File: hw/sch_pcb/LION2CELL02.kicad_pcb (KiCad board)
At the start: 2 copper layers, 80.8 x 60.5 mm, 100 parts, among them J1 USBC_USB4105-GF-A, J10 HEADER_2x01_PARALLEL, J11 HEADER_1x02, J12 HEADER_2x05_PARALLEL, J2 CONN1_1, J3 CONN1_1, J4 JUMP_4X2, J6 HEADER_2x01_PARALLEL, J7 HEADER_2x01_PARALLEL, J8 CONN1_1, J9 CONN1_1, Q1 DMT31M7LPS, Q2 AP2305AGN-HF-3, Q3 DMT31M7LPS, Q5 DMT31M7LPS, SW1 SW_Push, SW2 SW_Push, U1 BQ25792RQMR1, U2 LMR14050, U3 BQ40z50-R2

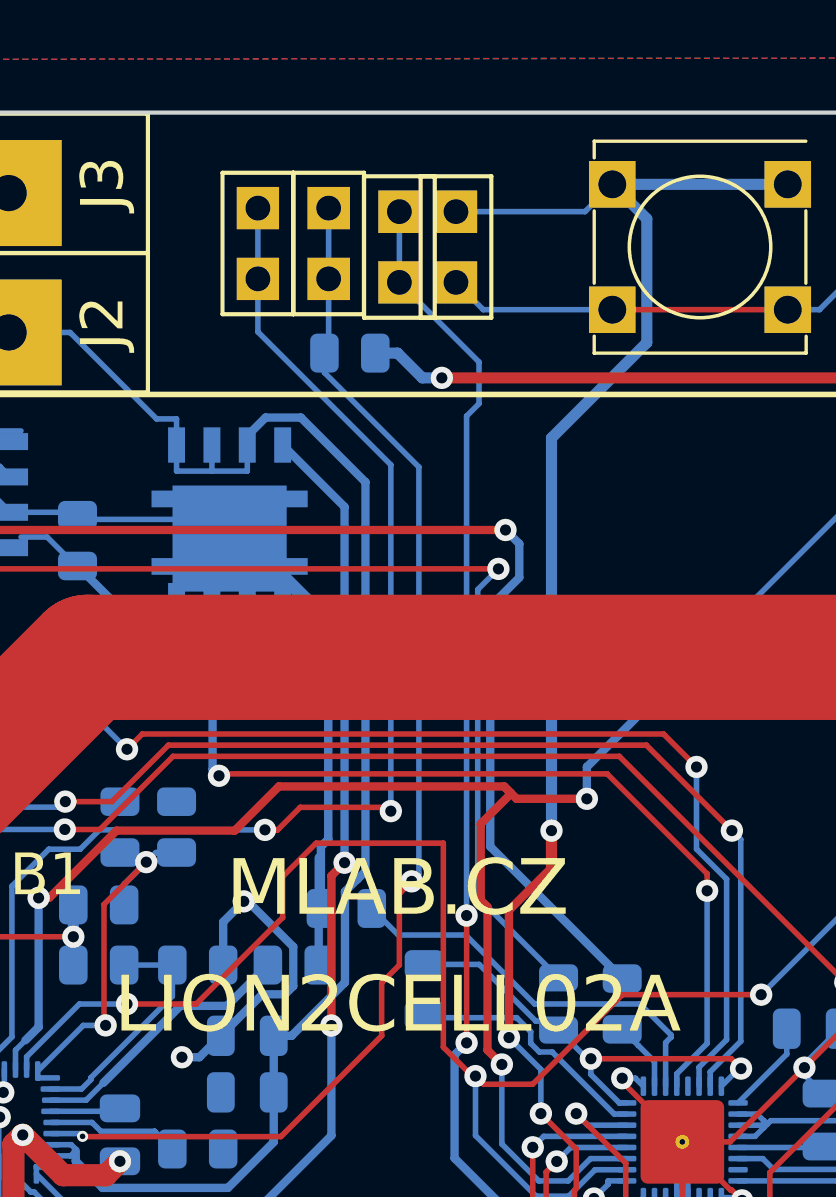
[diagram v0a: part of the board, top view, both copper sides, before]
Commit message: Reduce complexity of layout.
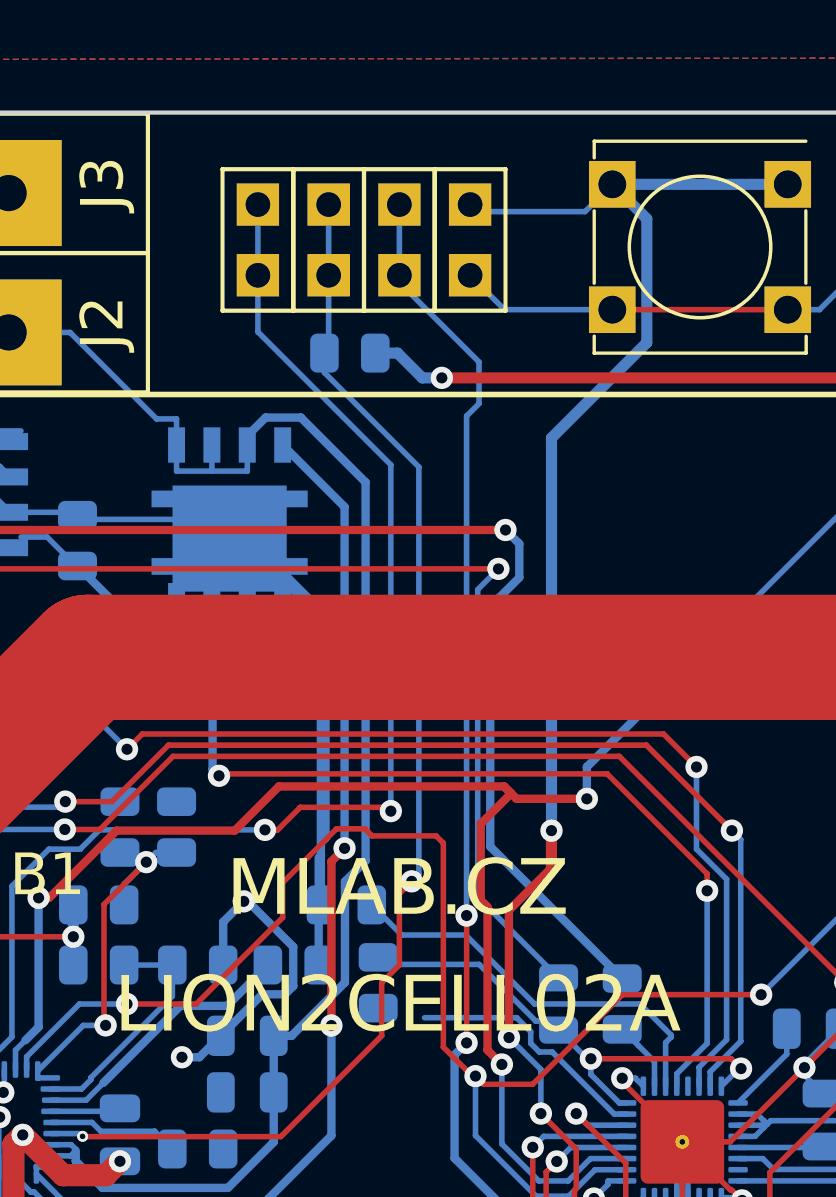
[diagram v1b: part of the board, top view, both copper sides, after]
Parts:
- moved TH4 1.67 mm to (147.7, 106.0)
- moved J11 0.57 mm to (151.0, 79.3)
- moved J10 0.25 mm to (148.5, 79.3)
- moved R24 0.13 mm to (146.6, 103.2)
- moved J6 0.13 mm to (146.0, 79.3)
- moved J7 0.13 mm to (143.4, 79.3)
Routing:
- net /Fuel Gauge/BAT: track 15.7 -> 17.5 mm
- net Net-(U3-~{PRES/SHDWN}): track 56.4 -> 55.6 mm

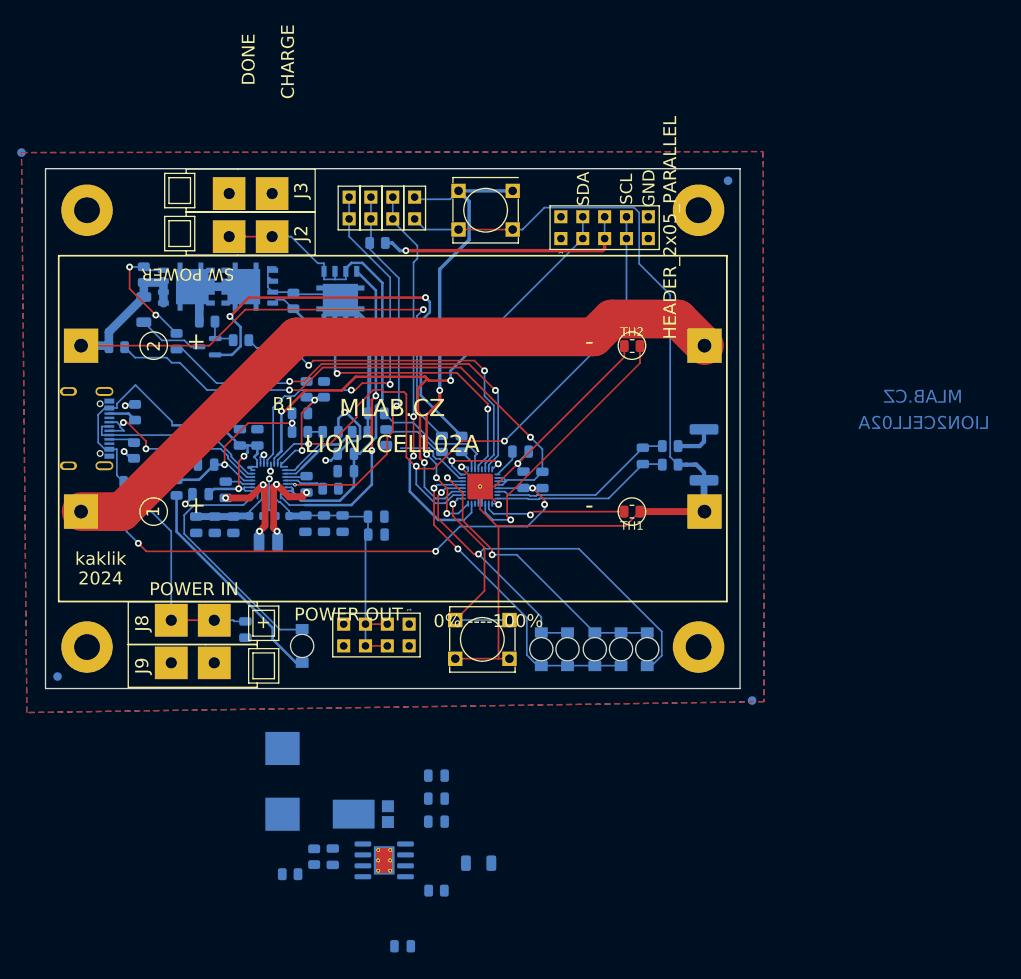
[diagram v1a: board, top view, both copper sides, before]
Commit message: Cleanup routing. Adding 5V output connector.
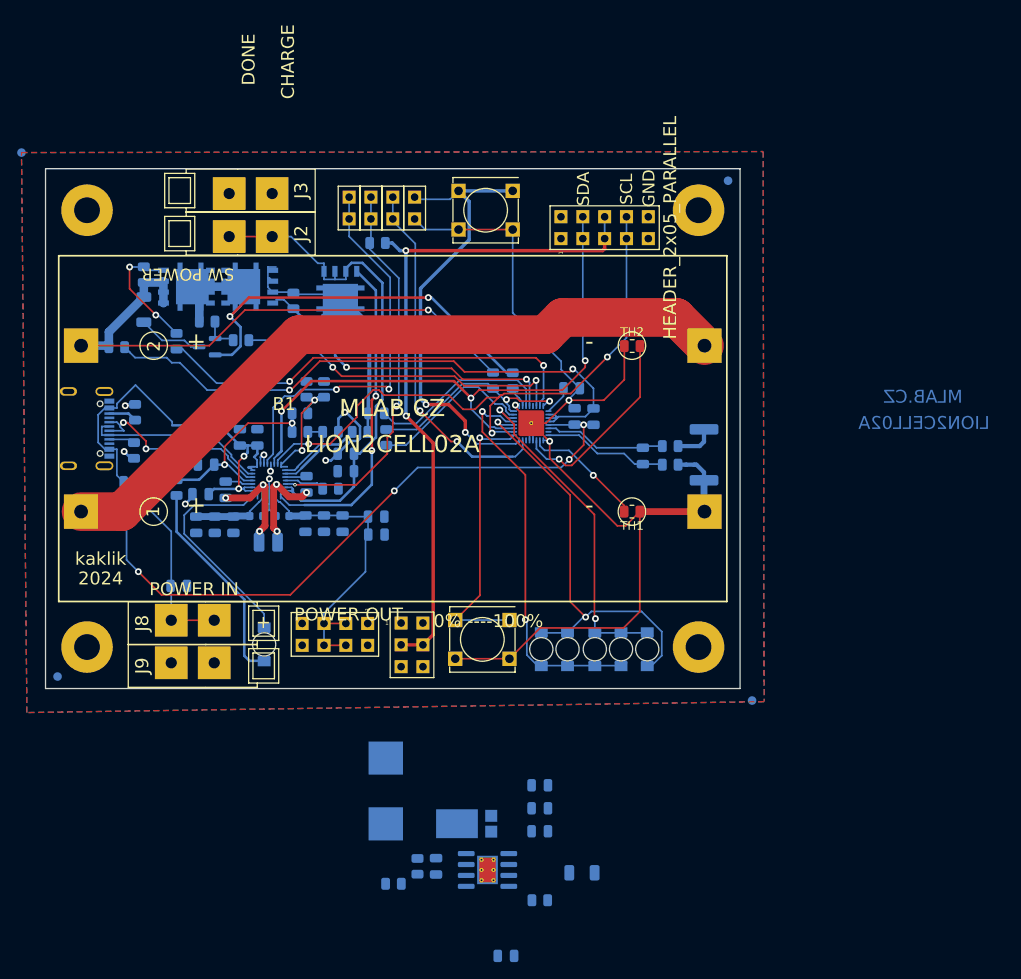
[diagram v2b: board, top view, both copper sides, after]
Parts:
- added J5: HEADER_2x03_PARALLEL, Mlab_Pin_Headers:Straight_2x03, F.Cu at (150.7, 130.1)
- moved C38 12.1 mm to (153.5, 155.9)
- moved R13 12.1 mm to (151.4, 155.9)
- moved C15 12.1 mm to (170.5, 156.7)
- moved C35 12.1 mm to (165.6, 151.8)
- moved D2 12.1 mm to (157.1, 150.9)
- moved L2 12.1 mm to (147.7, 147.1)
- moved R10 12.1 mm to (148.6, 157.9)
- moved U2 12.1 mm to (159.5, 156.3)
- moved C22 12.1 mm to (165.6, 146.5)
- moved C23 12.1 mm to (165.6, 149.1)
- moved C36 12.1 mm to (161.7, 166.3)
- moved R12 12.1 mm to (165.6, 159.8)
- moved C18 9.46 mm to (169.6, 103.6)
- moved D6 9.46 mm to (160.2, 99.4)
- moved R20 9.46 mm to (162.4, 99.4)
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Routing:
- net +3.3V: track 29.7 -> 79.9 mm, vias 1 -> 2
- net GND1: track 159.0 -> 132.7 mm
- net Net-(U3-VC1): track 61.8 -> 74.9 mm
- net /Fuel Gauge/SDA: track 81.2 -> 70.8 mm
- net Net-(U3-PTC): track 8.93 -> 19.2 mm
- net Net-(U3-~{DISP}): track 24.2 -> 32.9 mm
- net Net-(D1-A): track 57.5 -> 49.4 mm
- net Net-(U3-TS2): track 31.1 -> 23.1 mm
- net /Fuel Gauge/BAT: track 17.5 -> 25.1 mm
- net /Fuel Gauge/SR-: track 21.5 -> 14.0 mm
- net Net-(D1-K): track 38.4 -> 45.7 mm
- net Net-(U3-PACK): track 14.6 -> 21.5 mm
- net /Fuel Gauge/SR+: track 20.8 -> 14.6 mm
- net /Fuel Gauge/B+: track 75.1 -> 70.0 mm
- net /Fuel Gauge/VCOM: track 62.5 -> 57.6 mm
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
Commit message: Syncing board with schematics. Roughly placing the switching regulator.
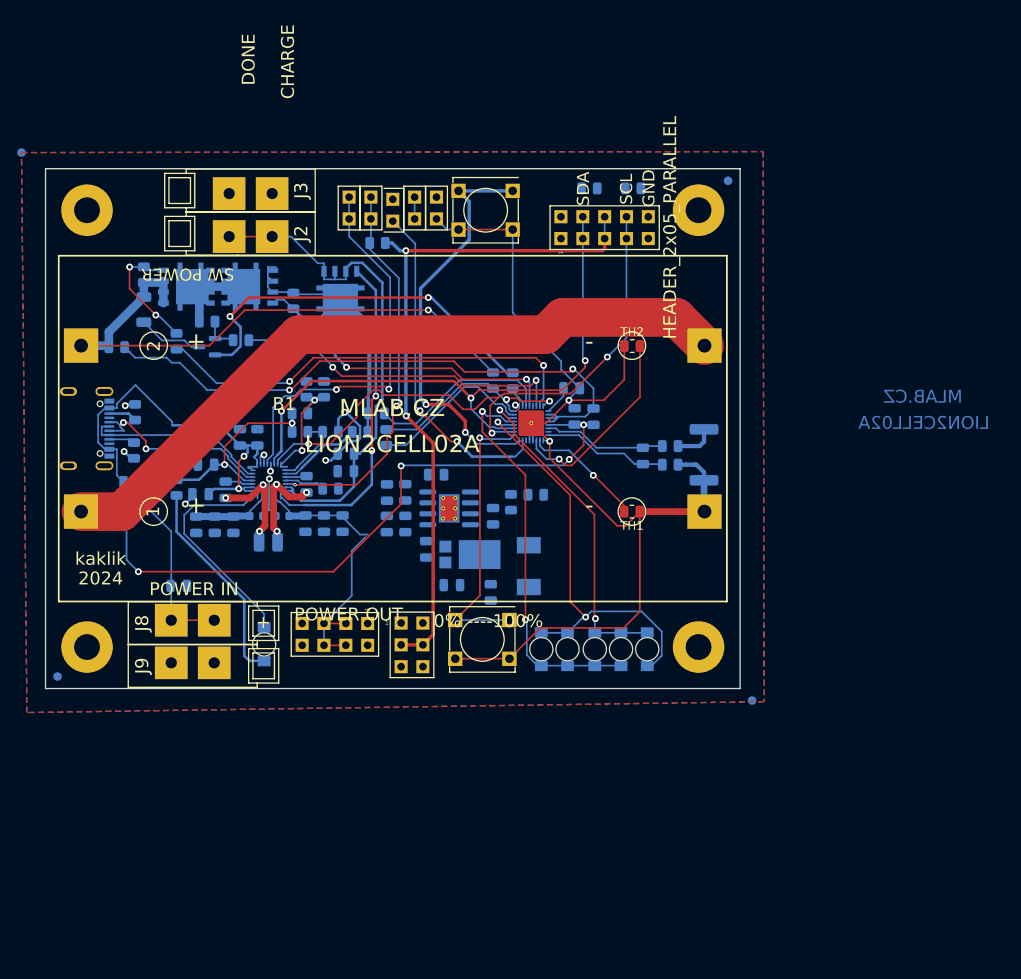
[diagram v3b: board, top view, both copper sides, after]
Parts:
- removed C15: 10uF, Capacitor_SMD:C_1206_3216Metric
- removed C22: 100nF, Capacitor_SMD:C_0805_2012Metric
- added C12: 1uF, Capacitor_SMD:C_0805_2012Metric, B.Cu at (150.0, 112.4)
- added C13: 10uF, Capacitor_SMD:C_0805_2012Metric, B.Cu at (150.0, 116.1)
- added JP1: Jumper_2_Open, Mlab_Pin_Headers:Straight_2x01, F.Cu at (148.5, 79.6)
- added R14: 10k, Resistor_SMD:R_0805_2012Metric, B.Cu at (176.4, 77.1)
- added R15: 10k, Resistor_SMD:R_0805_2012Metric, B.Cu at (171.4, 77.1)
- L2: value HCI1050-5R5 -> 2.2uH; footprint Inductor_SMD:L_Wuerth_HCI-1050 -> Inductor_SMD:L_Vishay_IHLP-2020
- R12: value 59k -> 15k8
- R13: value 15k -> 10k
- R9: value 6.04k -> 8k2
- moved R12 50.9 mm to (153.5, 110.4), turned to 0 degrees
- moved R10 48.2 mm to (165.1, 112.7), turned to 180 degrees
- moved R13 43.7 mm to (162.2, 113.6), turned to -90 degrees
- moved C36 42.3 mm to (159.9, 124.0), turned to -90 degrees
- moved U2 42.3 mm to (155.1, 114.3), turned to 0 degrees
- moved C38 41.3 mm to (160.2, 115.2), turned to -90 degrees
- moved C23 32.9 mm to (152.4, 119.0), turned to -90 degrees
- moved D2 31.3 mm to (157.5, 119.6), turned to 180 degrees
- moved L2 31.0 mm to (164.3, 121.0), turned to -90 degrees
- moved C35 30.4 mm to (155.4, 123.2)
- moved C8 5.04 mm to (147.8, 112.4), turned to 90 degrees
- moved J11 2.54 mm to (153.6, 79.3)
- moved J10 2.54 mm to (151.0, 79.3)
- moved C7 1.50 mm to (147.8, 116.1), turned to -90 degrees
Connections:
- C35 pad 1: +3.3V -> buck_out
- C36 pad 1: +3.3V -> buck_out
- J5 pad 3: +3.3V -> buck_out
- J5 pad 4: +3.3V -> buck_out
- L2 pad 2: +3.3V -> buck_out
- R10 pad 1: +3.3V -> buck_out
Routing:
- net Net-(U3-~{PRES/SHDWN}): track 53.2 -> 47.9 mm
- net GND1: track 132.7 -> 130.2 mm
- net /Power Input/System_load: track 34.0 -> 32.8 mm

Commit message: Routed switching regulator Starting of layout cleanup. Uniforming of charger and switching regulator inductors.
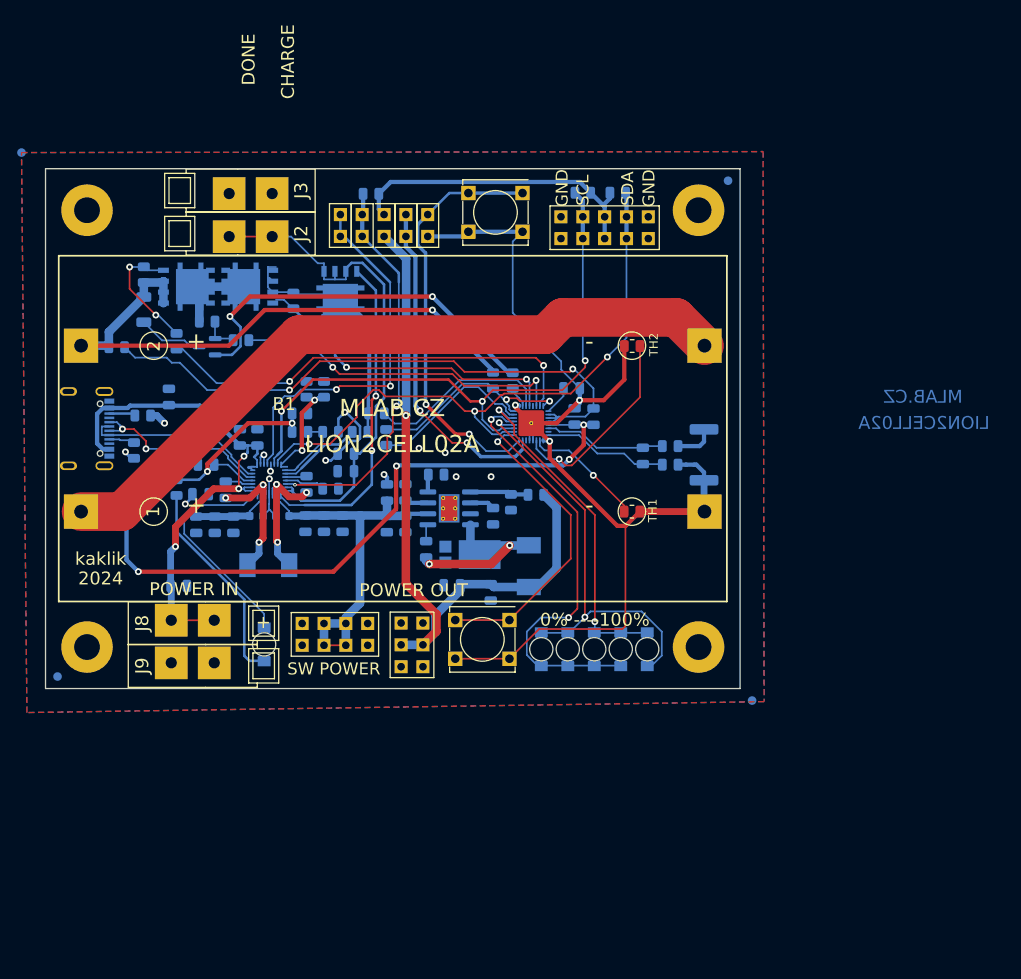
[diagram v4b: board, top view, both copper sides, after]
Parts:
- L1: value 1uH -> 2.2uH; footprint Inductor_SMD:L_1008_2520Metric -> Inductor_SMD:L_Vishay_IHLP-2020
- R10: value 91k -> 44k2
- moved C1 10.8 mm to (122.5, 101.3), turned to 90 degrees
- moved R11 5.77 mm to (146.0, 77.7)
- moved L1 2.67 mm to (134.0, 120.9)
- moved J11 2.27 mm to (152.6, 81.4)
- moved J6 2.27 mm to (144.9, 81.4)
- moved J10 2.27 mm to (150.0, 81.4)
- moved J7 2.27 mm to (142.4, 81.4)
- moved JP1 2.05 mm to (147.5, 81.4)
- moved R14 1.85 mm to (174.7, 77.6)
- moved SW1 1.17 mm to (160.4, 79.9)
- moved R1 0.97 mm to (119.4, 103.5), turned to 180 degrees
- moved R15 0.92 mm to (170.6, 77.6)
- moved D5 0.06 mm to (171.9, 130.7)
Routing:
- net buck_out: track 0.00 -> 83.5 mm, vias 0 -> 1
- net +3.3V: track 79.9 -> 36.2 mm, vias 2 -> 0
- net Net-(D2-K): track 0.00 -> 18.2 mm, vias 0 -> 2
- net /Power Input/System_load: track 32.8 -> 48.8 mm
- net Net-(U3-~{DISP}): track 32.9 -> 42.0 mm
- net Net-(U2-FB): track 0.00 -> 6.76 mm
- net VBUS: track 72.5 -> 67.4 mm, vias 2 -> 3
- net Net-(D1-K): track 45.7 -> 49.9 mm
- net /Power Input/REGN: track 24.6 -> 28.5 mm
- net Net-(U1-SW1): track 13.3 -> 16.3 mm
- net Net-(U1-SW2): track 12.7 -> 15.7 mm
- net /Fuel Gauge/SCL: track 70.4 -> 73.3 mm
- net Net-(U2-SS): track 0.00 -> 2.88 mm
- net Net-(U1-nQON): track 45.8 -> 43.7 mm
- net Net-(U2-RT/SYNC): track 0.00 -> 1.96 mm
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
